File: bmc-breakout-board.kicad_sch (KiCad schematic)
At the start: 5 parts

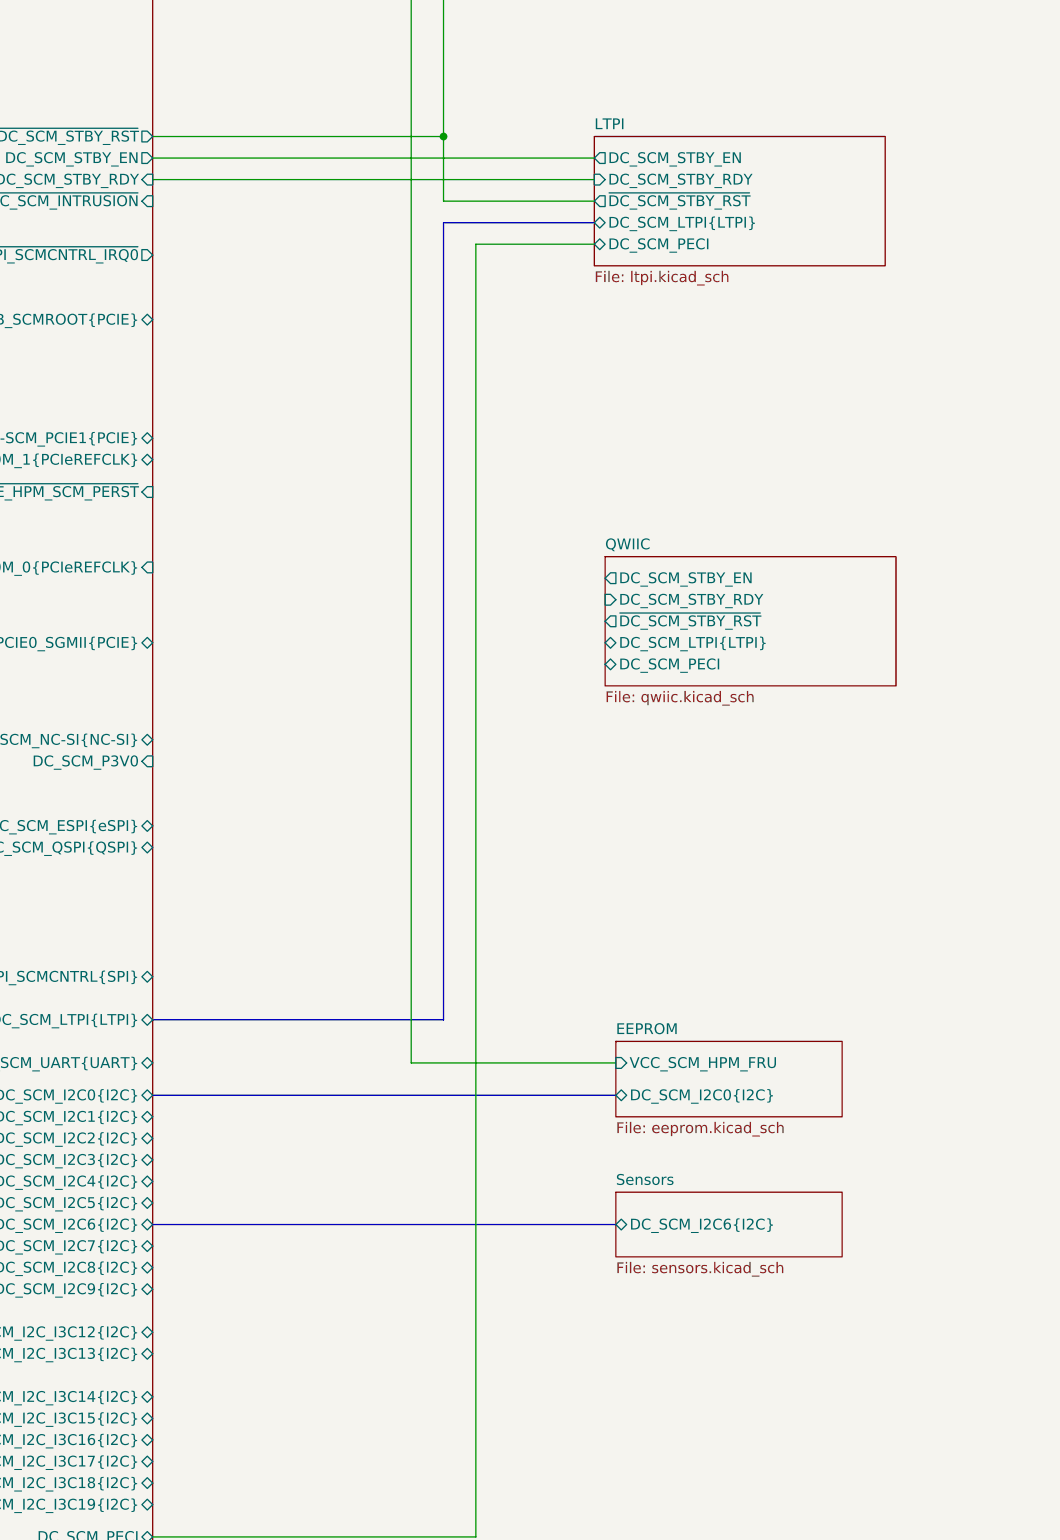
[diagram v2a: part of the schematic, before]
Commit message: [#92504] Connect QWIIC connector
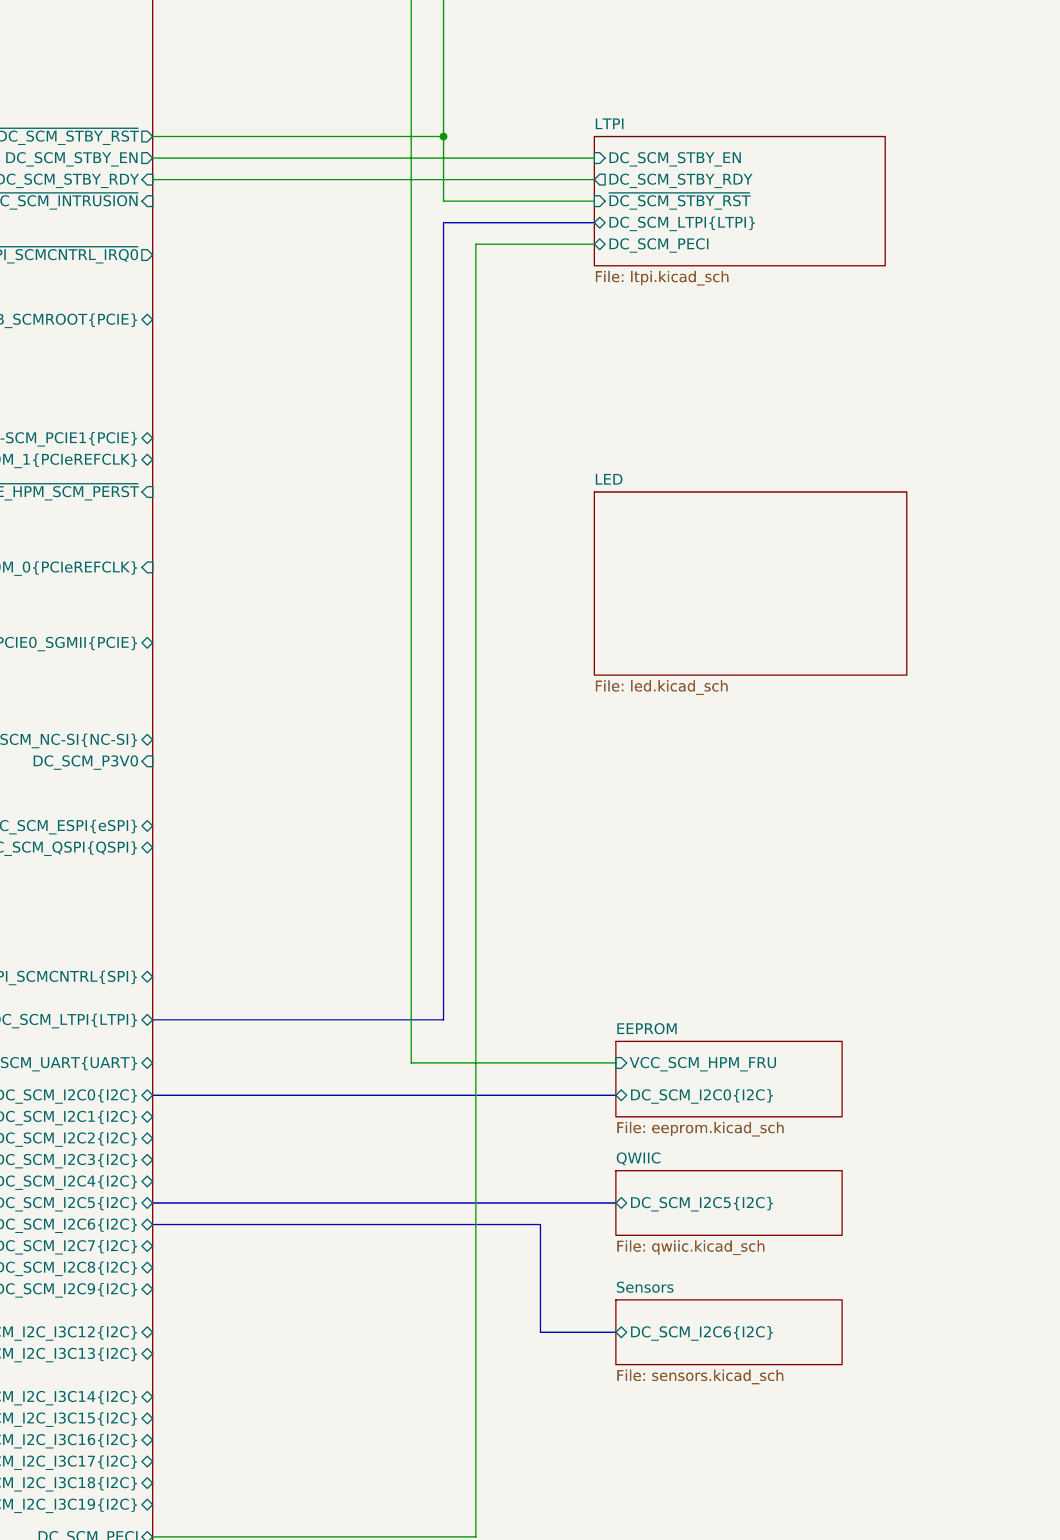
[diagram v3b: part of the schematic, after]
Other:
- added sheet LED (led.kicad_sch)
- sheet QWIIC ports: added DC_SCM_I2C5{I2C}; removed DC_SCM_LTPI{LTPI}, DC_SCM_PECI, DC_SCM_STBY_EN, DC_SCM_STBY_RDY, ~{DC_SCM_STBY_RST}
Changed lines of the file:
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@@
 	(bus
 		(pts
-			(xy 57.15 222.25) (xy 111.76 222.25)
+			(xy 102.87 222.25) (xy 57.15 222.25)
+		)
+		(stroke
+			(width 0)
+			(type default)
+		)
+	)
+	(bus
+		(pts
+			(xy 102.87 234.95) (xy 111.76 234.95)
 		)
 		(stroke
@@
 		)
 	)
+	(bus
+		(pts
+			(xy 102.87 234.95) (xy 102.87 222.25)
+		)
+		(stroke
+			(width 0)
+			(type default)
+		)
+	)
+	(bus
+		(pts
+			(xy 57.15 219.71) (xy 111.76 219.71)
+		)
+		(stroke
+			(width 0)
+			(type default)
+		)
+	)
 	(wire
 		(pts
@@
 			)
 		)
-		(pin "DC_SCM_STBY_EN" output
+		(pin "DC_SCM_STBY_EN" input
 			(at 109.22 96.52 180)
 			(effects
@@
 			)
 		)
-		(pin "DC_SCM_STBY_RDY" input
+		(pin "DC_SCM_STBY_RDY" output
 			(at 109.22 99.06 180)
 			(effects
@@
 			)
 		)
-		(pin "~{DC_SCM_STBY_RST}" output
+		(pin "~{DC_SCM_STBY_RST}" input
 			(at 109.22 101.6 180)
 			(effects
@@
 	)
 	(sheet
-		(at 111.76 218.44)
+		(at 109.22 135.89)
+		(size 36.83 21.59)
+		(exclude_from_sim no)
+		(in_bom yes)
+		(on_board yes)
+		(dnp no)
+		(fields_autoplaced yes)
+		(stroke
+			(width 0.1524)
+			(type solid)
+		)
+		(fill
+			(color 0 0 0 0.0000)
+		)
+		(property "Sheetname" "LED"
+			(at 109.22 135.1784 0)
+			(effects
+				(font
+					(size 1.27 1.27)
+				)
+				(justify left bottom)
+			)
+		)
+		(property "Sheetfile" "led.kicad_sch"
+			(at 109.22 158.0646 0)
+			(effects
+				(font
+					(size 1.27 1.27)
+				)
+				(justify left top)
+			)
+		)
+		(instances
+			(project "bmc-breakout-board"
+				(path "/5d67ef28-5805-4f87-b722-2926dabf7f6e"
+					(page "8")
+				)
+			)
+		)
+	)
+	(sheet
+		(at 111.76 231.14)
 		(size 26.67 7.62)
 		(exclude_from_sim no)
@@
 		)
 		(property "Sheetname" "Sensors"
-			(at 111.76 217.7284 0)
+			(at 111.76 230.4284 0)
 			(effects
 				(font
@@
 		)
 		(property "Sheetfile" "sensors.kicad_sch"
-			(at 111.76 226.6446 0)
+			(at 111.76 239.3446 0)
 			(effects
 				(font
@@
 		)
 		(pin "DC_SCM_I2C6{I2C}" bidirectional
-			(at 111.76 222.25 180)
+			(at 111.76 234.95 180)
 			(effects
 				(font
@@
 	)
 	(sheet
-		(at 110.49 143.51)
-		(size 34.29 15.24)
+		(at 111.76 215.9)
+		(size 26.67 7.62)
 		(exclude_from_sim no)
 		(in_bom yes)
@@
 		)
 		(property "Sheetname" "QWIIC"
-			(at 110.49 142.7984 0)
+			(at 111.76 215.1884 0)
 			(effects
 				(font
@@
 		)
 		(property "Sheetfile" "qwiic.kicad_sch"
-			(at 110.49 159.3346 0)
+			(at 111.76 224.1046 0)
 			(effects
 				(font
@@
 			)
 		)
-		(pin "DC_SCM_LTPI{LTPI}" bidirectional
-			(at 110.49 153.67 180)
-			(effects
-				(font
-					(size 1.27 1.27)
-				)
-				(justify left)
-			)
-		)
-		(pin "DC_SCM_PECI" bidirectional
-			(at 110.49 156.21 180)
-			(effects
-				(font
-					(size 1.27 1.27)
-				)
-				(justify left)
-			)
-		)
-		(pin "DC_SCM_STBY_EN" output
-			(at 110.49 146.05 180)
-			(effects
-				(font
-					(size 1.27 1.27)
-				)
-				(justify left)
-			)
-		)
-		(pin "DC_SCM_STBY_RDY" input
-			(at 110.49 148.59 180)
-			(effects
-				(font
-					(size 1.27 1.27)
-				)
-				(justify left)
-			)
-		)
-		(pin "~{DC_SCM_STBY_RST}" output
-			(at 110.49 151.13 180)
+		(pin "DC_SCM_I2C5{I2C}" bidirectional
+			(at 111.76 219.71 180)
 			(effects
 				(font

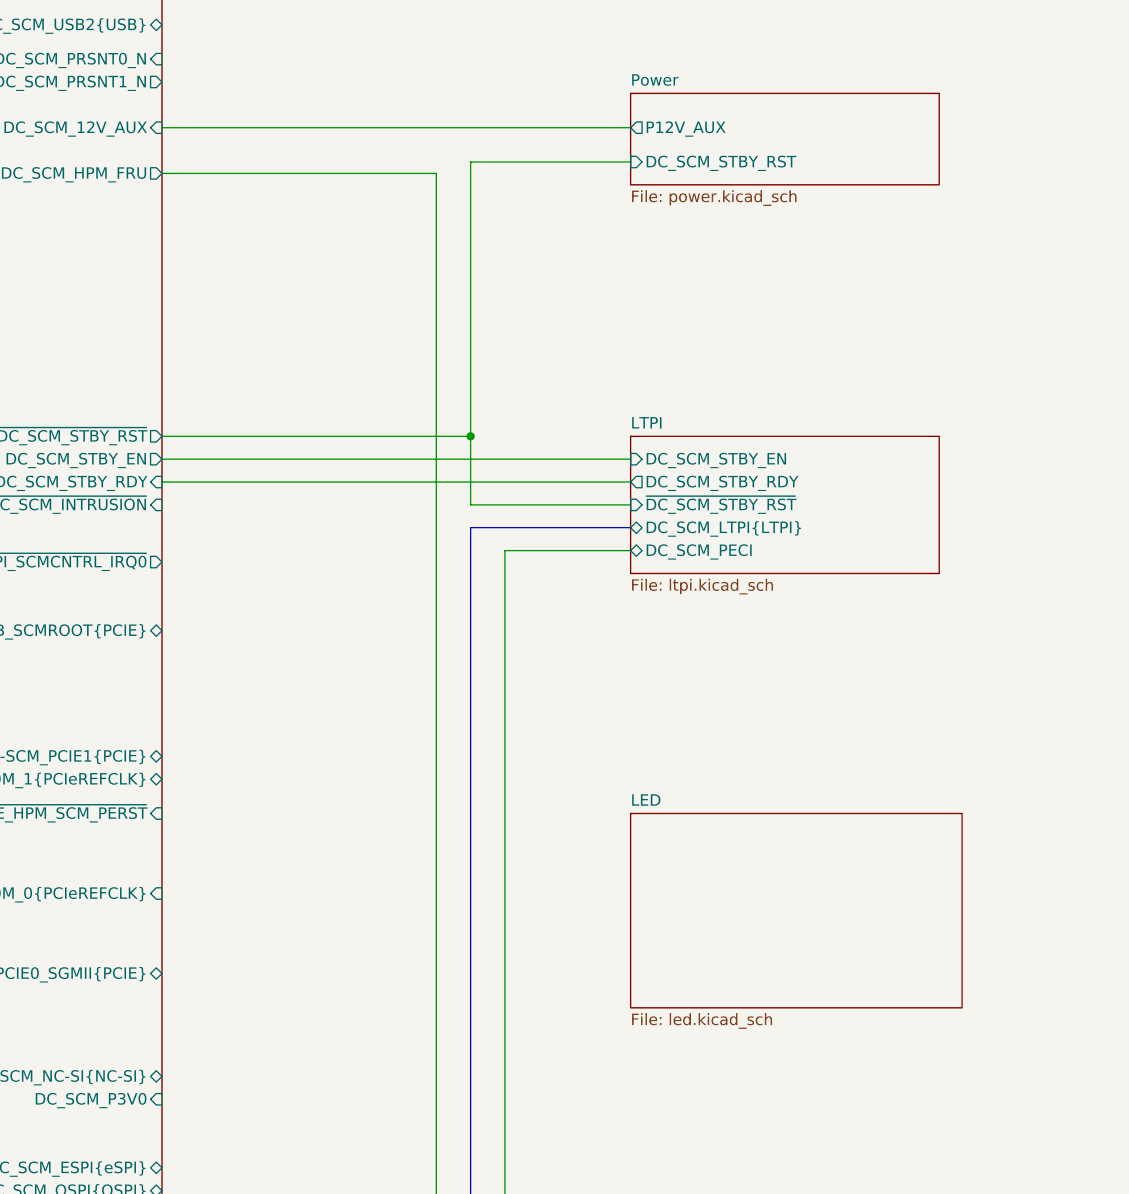
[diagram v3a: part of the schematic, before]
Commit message: [#92504] Connect Indicator LEDs
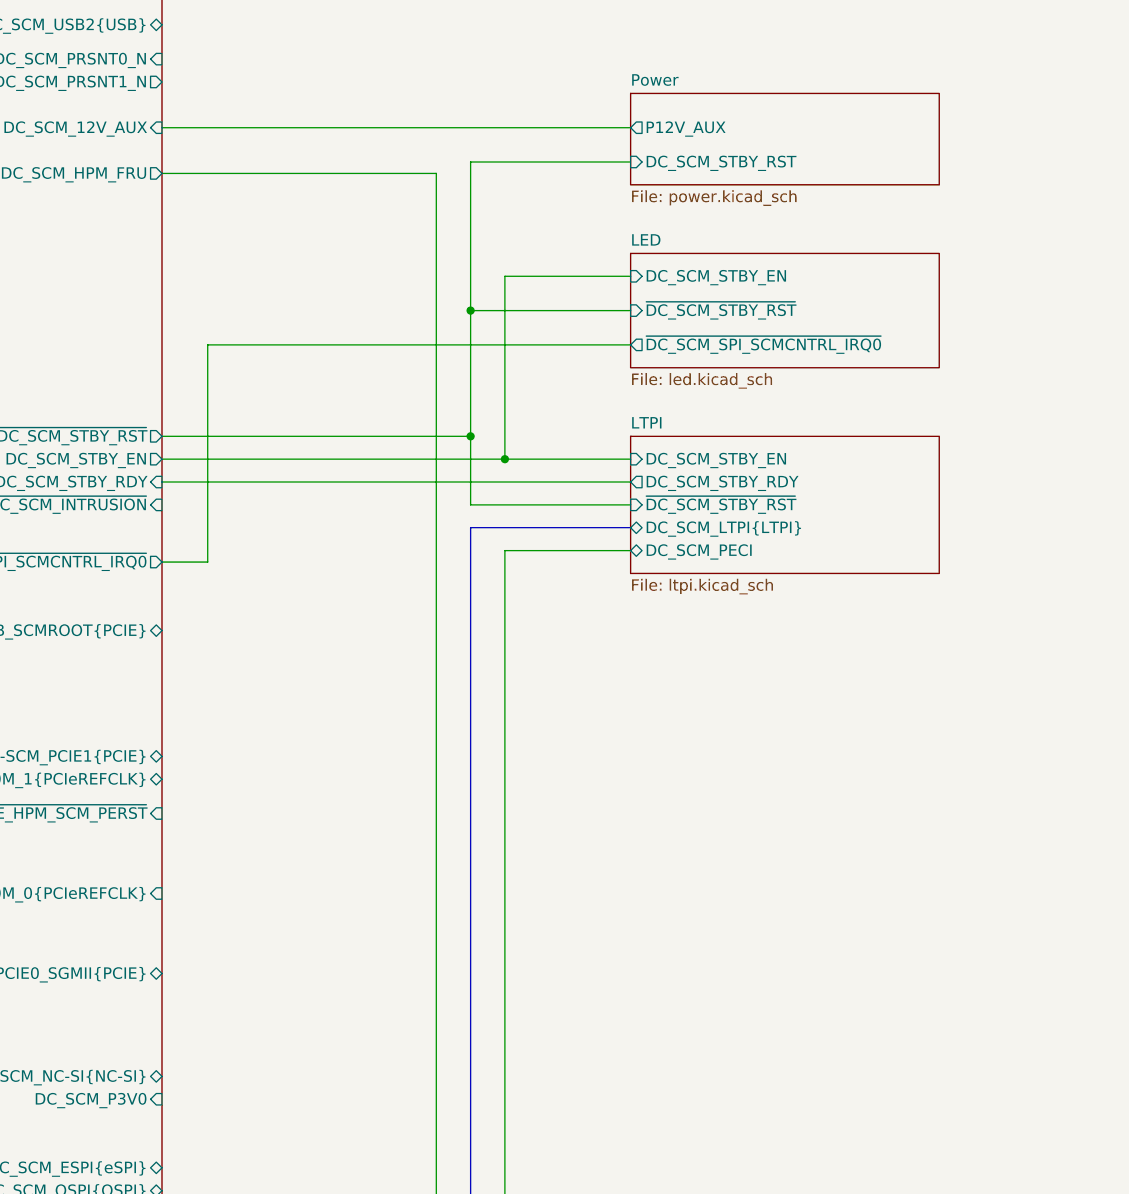
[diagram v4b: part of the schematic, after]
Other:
- sheet LED ports: added DC_SCM_STBY_EN, ~{DC_SCM_SPI_SCMCNTRL_IRQ0}, ~{DC_SCM_STBY_RST}; removed none
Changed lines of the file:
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@@
+	)
+	(junction
+		(at 91.44 80.01)
+		(diameter 0)
+		(color 0 0 0 0)
 	)
 	(junction
@@
 		(color 0 0 0 0)
 	)
+	(junction
+		(at 95.25 96.52)
+		(diameter 0)
+		(color 0 0 0 0)
+	)
 	(bus
 		(pts
@@
 		)
 	)
+	(wire
+		(pts
+			(xy 91.44 80.01) (xy 109.22 80.01)
+		)
+		(stroke
+			(width 0)
+			(type default)
+		)
+	)
 	(bus
 		(pts
@@
 		)
 	)
+	(wire
+		(pts
+			(xy 95.25 96.52) (xy 57.15 96.52)
+		)
+		(stroke
+			(width 0)
+			(type default)
+		)
+	)
+	(wire
+		(pts
+			(xy 95.25 76.2) (xy 95.25 96.52)
+		)
+		(stroke
+			(width 0)
+			(type default)
+		)
+	)
 	(bus
 		(pts
@@
 	(wire
 		(pts
+			(xy 62.23 83.82) (xy 109.22 83.82)
+		)
+		(stroke
+			(width 0)
+			(type default)
+		)
+	)
+	(wire
+		(pts
 			(xy 95.25 259.08) (xy 57.15 259.08)
 		)
@@
 	(wire
 		(pts
+			(xy 62.23 107.95) (xy 57.15 107.95)
+		)
+		(stroke
+			(width 0)
+			(type default)
+		)
+	)
+	(wire
+		(pts
 			(xy 57.15 99.06) (xy 109.22 99.06)
+		)
+		(stroke
+			(width 0)
+			(type default)
+		)
+	)
+	(wire
+		(pts
+			(xy 109.22 76.2) (xy 95.25 76.2)
 		)
 		(stroke
@@
 	(wire
 		(pts
-			(xy 91.44 93.98) (xy 57.15 93.98)
+			(xy 91.44 80.01) (xy 91.44 93.98)
 		)
 		(stroke
@@
 	(wire
 		(pts
-			(xy 109.22 96.52) (xy 57.15 96.52)
+			(xy 91.44 93.98) (xy 57.15 93.98)
+		)
+		(stroke
+			(width 0)
+			(type default)
+		)
+	)
+	(wire
+		(pts
+			(xy 109.22 96.52) (xy 95.25 96.52)
+		)
+		(stroke
+			(width 0)
+			(type default)
+		)
+	)
+	(wire
+		(pts
+			(xy 62.23 83.82) (xy 62.23 107.95)
 		)
 		(stroke
@@
 	(wire
 		(pts
-			(xy 91.44 63.5) (xy 91.44 93.98)
+			(xy 91.44 63.5) (xy 91.44 80.01)
 		)
 		(stroke
@@
 	)
 	(sheet
-		(at 109.22 135.89)
-		(size 36.83 21.59)
+		(at 109.22 73.66)
+		(size 34.29 12.7)
 		(exclude_from_sim no)
 		(in_bom yes)
@@
 		)
 		(property "Sheetname" "LED"
-			(at 109.22 135.1784 0)
+			(at 109.22 72.9484 0)
 			(effects
 				(font
@@
 		)
 		(property "Sheetfile" "led.kicad_sch"
-			(at 109.22 158.0646 0)
+			(at 109.22 86.9446 0)
 			(effects
 				(font
@@
 			)
 		)
+		(pin "~{DC_SCM_SPI_SCMCNTRL_IRQ0}" output
+			(at 109.22 83.82 180)
+			(effects
+				(font
+					(size 1.27 1.27)
+				)
+				(justify left)
+			)
+		)
+		(pin "~{DC_SCM_STBY_RST}" input
+			(at 109.22 80.01 180)
+			(effects
+				(font
+					(size 1.27 1.27)
+				)
+				(justify left)
+			)
+		)
+		(pin "DC_SCM_STBY_EN" input
+			(at 109.22 76.2 180)
+			(effects
+				(font
+					(size 1.27 1.27)
+				)
+				(justify left)
+			)
+		)
